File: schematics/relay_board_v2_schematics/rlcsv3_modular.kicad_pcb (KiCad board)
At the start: 2 copper layers, 45 x 75 mm, 46 parts, among them J1 Programming Header, P1 ACT_PWR, P2 ACT_PWR, P3 ACTUATOR, Q1 MMBF170, Q2 MMBF170, U1 SPST_POWER_RELAY, U2 PIC16F1826-ISO, U3 dpdt_relay, U4 INA180A1, U5 CONN_01x05, U6 INA180A1, U7 CONN_01x05

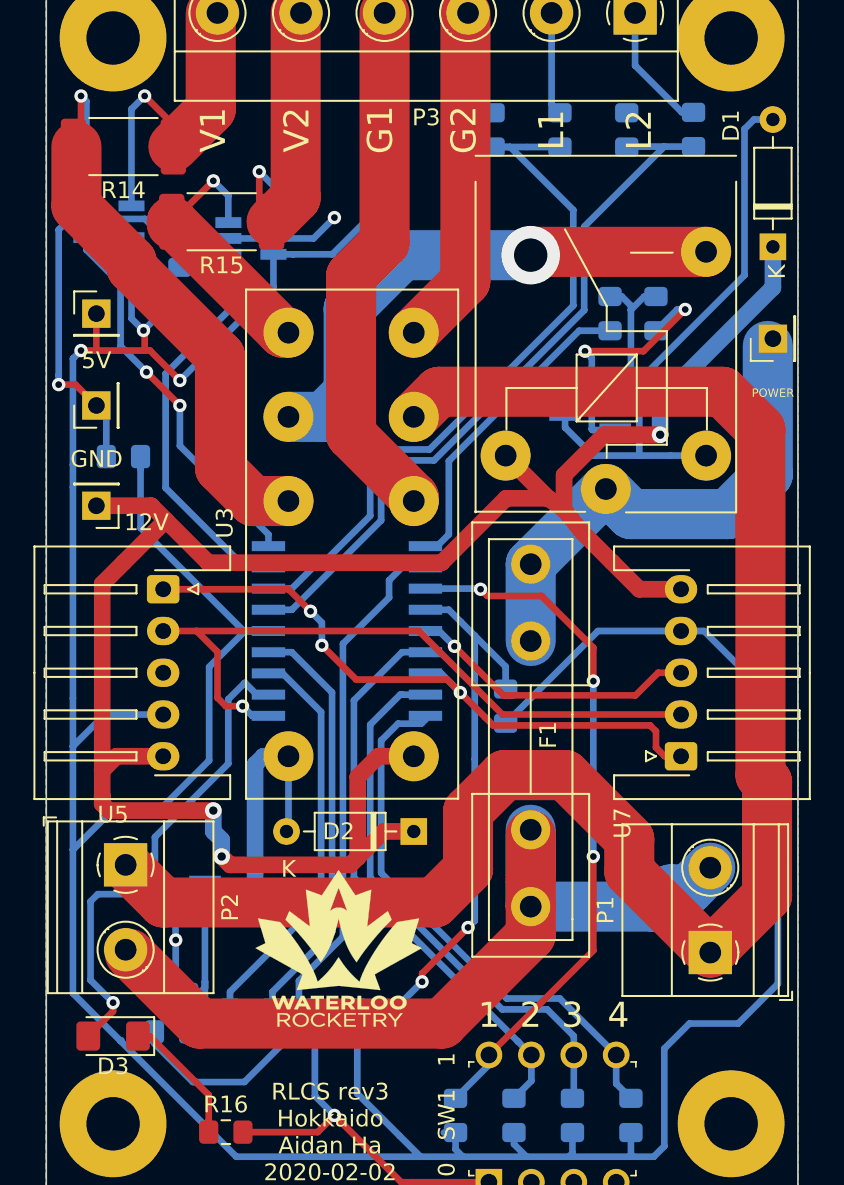
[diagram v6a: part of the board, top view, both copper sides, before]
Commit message: Add more fix for silkscreen
Signed-off-by: AIDAN HA <qbha@edu.uwaterloo.ca>
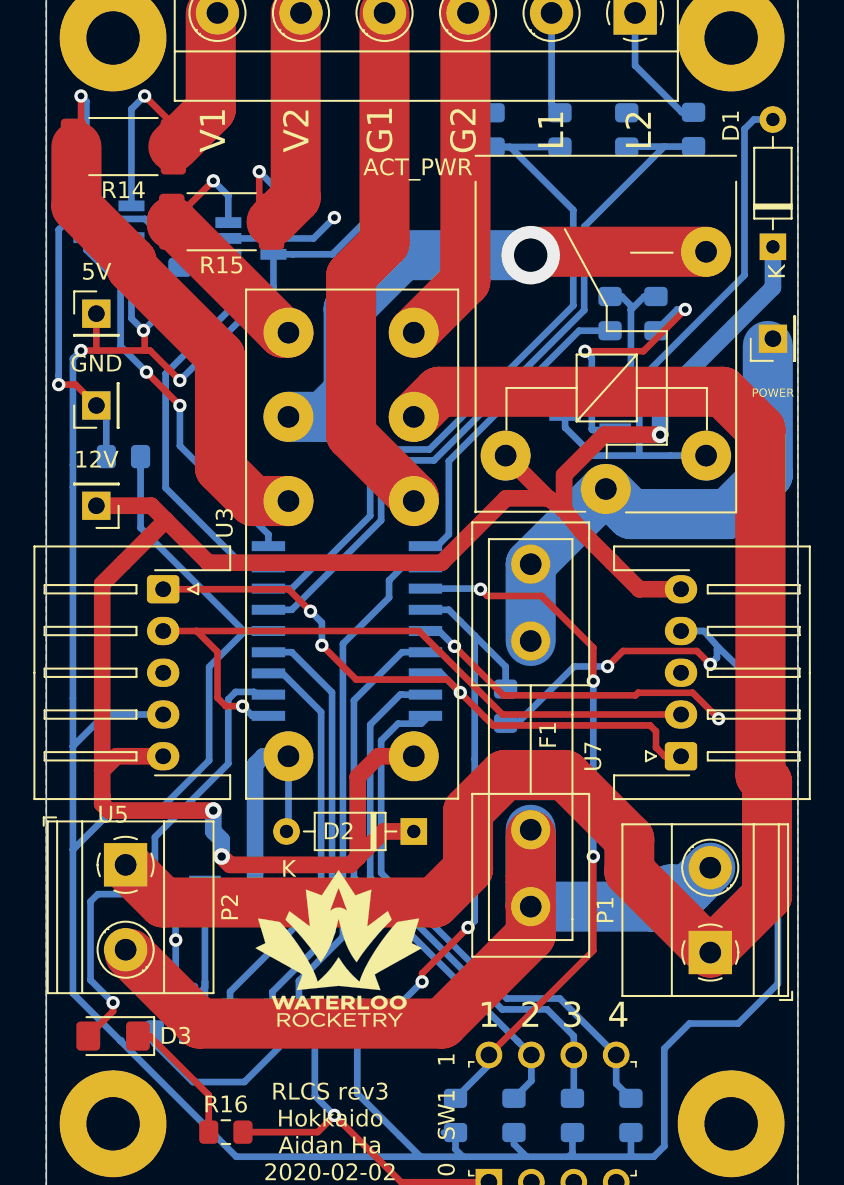
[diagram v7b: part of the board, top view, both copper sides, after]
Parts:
- renumbered P3 to ACT_PWR
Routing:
- net +5V: track 224.7 -> 227.5 mm, vias 3 -> 5
- net GND: track 198.0 -> 200.4 mm, vias 7 -> 8
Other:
- board text added: "~MCLR 5V"
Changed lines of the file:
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@@
   (general
     (thickness 1.6)
-    (drawings 15)
-    (tracks 460)
+    (drawings 16)
+    (tracks 472)
     (zones 0)
     (modules 46)
@@
     (visible_elements 7FFFF7FF)
     (pcbplotparams
-      (layerselection 0x010fc_ffffffff)
+      (layerselection 0x010f0_ffffffff)
       (usegerberextensions true)
       (usegerberattributes false)
@@
     (tags "LED handsolder")
     (attr smd)
-    (fp_text reference D3 (at 0 -1.82) (layer F.SilkS)
+    (fp_text reference D3 (at -3.75 0) (layer F.SilkS)
       (effects (font (size 1 1) (thickness 0.15)))
     )
@@
   (module rlcs:PinHeader_5x2.54_SMD_90deg_952-3198-1-ND (layer B.Cu)
     (at 141 132.5)
-    (fp_text reference J1 (at 12.5 0.75 270) (layer B.SilkS)
+    (fp_text reference J1 (at -0.25 1.25 270) (layer B.SilkS)
       (effects (font (size 1 1) (thickness 0.15)) (justify mirror))
     )
@@
     (descr "Terminal Block Phoenix MKDS-1,5-6, 6 pins, pitch 5mm, size 30x9.8mm^2, drill diamater 1.3mm, pad diameter 2.6mm, see http://www.farnell.com/datasheets/100425.pdf, script-generated using https://github.com/pointhi/kicad-footprint-generator/scripts/TerminalBlock_Phoenix")
     (tags "THT Terminal Block Phoenix MKDS-1,5-6 pitch 5mm size 30x9.8mm^2 drill 1.3mm pad 2.6mm")
-    (fp_text reference P3 (at 12.5 -6.26) (layer F.SilkS)
+    (fp_text reference ACT_PWR (at 13 -9.25) (layer F.SilkS)
       (effects (font (size 1 1) (thickness 0.15)))
     )
@@
     (descr "Through hole straight socket strip, 1x01, 2.54mm pitch, single row")
     (tags "Through hole socket strip THT 1x01 2.54mm single row")
-    (fp_text reference GND (at -3.21 0.01 180) (layer F.SilkS)
+    (fp_text reference GND (at 2.5 0 180) (layer F.SilkS)
       (effects (font (size 1 1) (thickness 0.15)))
     )
@@
     (descr "Through hole straight socket strip, 1x01, 2.54mm pitch, single row")
     (tags "Through hole socket strip THT 1x01 2.54mm single row")
-    (fp_text reference 12V (at -3 -1) (layer F.SilkS)
+    (fp_text reference 12V (at 0 2.75) (layer F.SilkS)
       (effects (font (size 1 1) (thickness 0.15)))
     )
@@
     (descr "Through hole straight socket strip, 1x01, 2.54mm pitch, single row")
     (tags "Through hole socket strip THT 1x01 2.54mm single row")
-    (fp_text reference 5V (at 0 2.8) (layer F.SilkS)
+    (fp_text reference 5V (at 0 -2.5) (layer F.SilkS)
       (effects (font (size 1 1) (thickness 0.15)))
     )
@@
     (descr "JST XH series connector, S5B-XH-A-1 (http://www.jst-mfg.com/product/pdf/eng/eXH.pdf), generated with kicad-footprint-generator")
     (tags "connector JST XH horizontal")
-    (fp_text reference U7 (at -4 -3.5 90) (layer F.SilkS)
+    (fp_text reference U7 (at 0 -5.25 90) (layer F.SilkS)
       (effects (font (size 1 1) (thickness 0.15)))
     )
@@
       (rotate (xyz 0 0 0))
     )
+  )
+  (gr_text "~MCLR 5V" (at 154 133.25 90) (layer B.SilkS)
+    (effects (font (size 1 1) (thickness 0.15)) (justify mirror))
   )
   (gr_text 1 (at 156.5 132.5) (layer F.SilkS)
@@
   (via (at 154.436166 110.417836) (size 0.8) (drill 0.4) (layers F.Cu B.Cu) (net 5))
   (segment (start 152.7 109.5) (end 153.51833 109.5) (width 0.4) (layer B.Cu) (net 5))
-  (segment (start 166.625 112) (end 168 112) (width 0.4) (layer F.Cu) (net 5))
-  (segment (start 165.270999 113.354001) (end 166.625 112) (width 0.4) (layer F.Cu) (net 5))
   (segment (start 157.372331 113.354001) (end 165.270999 113.354001) (width 0.4) (layer F.Cu) (net 5))
   (segment (start 154.436166 110.417836) (end 157.372331 113.354001) (width 0.4) (layer F.Cu) (net 5))
@@
   (segment (start 146.25 139.5) (end 147.25 138.5) (width 0.4) (layer F.Cu) (net 5))
   (segment (start 141.775 139.5) (end 146.25 139.5) (width 0.4) (layer F.Cu) (net 5))
+  (via (at 170.25 114.75) (size 0.8) (drill 0.4) (layers F.Cu B.Cu) (net 5))
+  (segment (start 165.42901 113.19599) (end 168.69599 113.19599) (width 0.4) (layer F.Cu) (net 5))
+  (segment (start 168.69599 113.19599) (end 170.25 114.75) (width 0.4) (layer F.Cu) (net 5))
+  (segment (start 165.270999 113.354001) (end 165.42901 113.19599) (width 0.4) (layer F.Cu) (net 5))
   (via (at 138 94.5) (size 0.8) (drill 0.4) (layers F.Cu B.Cu) (net 6))
-  (segment (start 163.025 109.5) (end 157.5 115.025) (width 0.4) (layer B.Cu) (net 6))
-  (segment (start 168 109.5) (end 163.025 109.5) (width 0.4) (layer B.Cu) (net 6))
   (segment (start 168 109.5) (end 167.647295 109.5) (width 0.4) (layer B.Cu) (net 6))
   (segment (start 154.5 139.525) (end 153.8 139.525) (width 0.4) (layer B.Cu) (net 6))
@@
   (segment (start 173.800009 130.617193) (end 171.417202 133) (width 0.4) (layer B.Cu) (net 6))
   (segment (start 168.5 133) (end 167 134.5) (width 0.4) (layer B.Cu) (net 6))
-  (segment (start 169.375 109.5) (end 173.800009 113.925009) (width 0.4) (layer B.Cu) (net 6))
   (segment (start 168 109.5) (end 169.375 109.5) (width 0.4) (layer B.Cu) (net 6))
   (segment (start 173.800009 113.925009) (end 173.800009 130.617193) (width 0.4) (layer B.Cu) (net 6))
@@
   (segment (start 141.377922 140.97) (end 134.453961 134.046039) (width 0.4) (layer B.Cu) (net 6))
   (segment (start 134.453961 134.046039) (end 131.595999 131.188077) (width 0.4) (layer B.Cu) (net 6))
+  (via (at 163.604 111.623017) (size 0.8) (drill 0.4) (layers F.Cu B.Cu) (net 6))
+  (segment (start 161.601983 111.623017) (end 163.604 111.623017) (width 0.4) (layer B.Cu) (net 6))
+  (segment (start 158.2 115.025) (end 161.601983 111.623017) (width 0.4) (layer B.Cu) (net 6))
+  (segment (start 157.5 115.025) (end 158.2 115.025) (width 0.4) (layer B.Cu) (net 6))
+  (segment (start 168.94599 110.69599) (end 169.75 111.5) (width 0.4) (layer F.Cu) (net 6))
+  (segment (start 164.531027 110.69599) (end 168.94599 110.69599) (width 0.4) (layer F.Cu) (net 6))
+  (via (at 169.75 111.5) (size 0.8) (drill 0.4) (layers F.Cu B.Cu) (net 6))
+  (segment (start 163.604 111.623017) (end 164.531027 110.69599) (width 0.4) (layer F.Cu) (net 6))
+  (segment (start 170.149999 110.600001) (end 170.25 110.5) (width 0.4) (layer B.Cu) (net 6))
+  (segment (start 170.149999 111.100001) (end 170.149999 110.600001) (width 0.4) (layer B.Cu) (net 6))
+  (segment (start 169.75 111.5) (end 170.149999 111.100001) (width 0.4) (layer B.Cu) (net 6))
+  (segment (start 170.25 110.5) (end 173.800009 113.925009) (width 0.4) (layer B.Cu) (net 6))
+  (segment (start 169.375 109.5) (end 170.25 110.5) (width 0.4) (layer B.Cu) (net 6))
   (segment (start 159 121.4) (end 159 126) (width 3) (layer B.Cu) (net 7))
   (segment (start 168.450001 124.969999) (end 169.75 123.67) (width 3) (layer B.Cu) (net 7))
@@
   (segment (start 133.086799 125.254001) (end 132.649999 125.690801) (width 0.4) (layer B.Cu) (net 35))
   (segment (start 140.895999 117.444801) (end 136.504001 121.836799) (width 0.4) (layer B.Cu) (net 35))
-  (segment (start 141.876078 112.61) (end 140.895999 113.590079) (width 0.4) (layer B.Cu) (net 35))
-  (segment (start 140.895999 113.590079) (end 140.895999 117.444801) (width 0.4) (layer B.Cu) (net 35))
-  (segment (start 141.9 112.61) (end 141.876078 112.61) (width 0.4) (layer B.Cu) (net 35))
   (via (at 134 131.75) (size 0.8) (drill 0.4) (layers F.Cu B.Cu) (net 35))
   (segment (start 136.413201 125.254001) (end 133.086799 125.254001) (width 0.4) (layer B.Cu) (net 35))
   (segment (start 136.504001 125.163201) (end 136.413201 125.254001) (width 0.4) (layer B.Cu) (net 35))
   (segment (start 136.504001 121.836799) (end 136.504001 125.163201) (width 0.4) (layer B.Cu) (net 35))
-  (segment (start 142.6 113.31) (end 141.9 112.61) (width 0.4) (layer B.Cu) (net 35))
   (segment (start 132.649999 125.690801) (end 132.649999 130.399999) (width 0.4) (layer B.Cu) (net 35))
-  (segment (start 143.3 113.31) (end 142.6 113.31) (width 0.4) (layer B.Cu) (net 35))
   (segment (start 134 132.2625) (end 132.5125 133.75) (width 0.4) (layer F.Cu) (net 35))
   (segment (start 134 131.75) (end 134 132.2625) (width 0.4) (layer F.Cu) (net 35))
+  (segment (start 141.340079 113.145999) (end 140.895999 113.590079) (width 0.4) (layer B.Cu) (net 35))
+  (segment (start 140.895999 113.590079) (end 140.895999 117.444801) (width 0.4) (layer B.Cu) (net 35))
+  (segment (start 142.435999 113.145999) (end 141.340079 113.145999) (width 0.4) (layer B.Cu) (net 35))
+  (segment (start 142.6 113.31) (end 142.435999 113.145999) (width 0.4) (layer B.Cu) (net 35))
+  (segment (start 143.3 113.31) (end 142.6 113.31) (width 0.4) (layer B.Cu) (net 35))
   (zone (net 5) (net_name GND) (layer F.Cu) (hatch edge 0.508)
     (connect_pads (clearance 0.7))
